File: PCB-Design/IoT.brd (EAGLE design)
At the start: 161.3 x 101.3 mm, 10 parts, among them M2 ARDUINO-NANO-3.0, M3 WIRELESS-NRF24L01

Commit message: WIP: PCB routing
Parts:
- moved U$1 49.6 mm to (44.5, 53.3)
- moved U$2 49.5 mm to (6.35, 53.3)
- moved U$4 49.5 mm to (31.8, 53.3)
- moved U$3 49.5 mm to (19.1, 53.3)
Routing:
- net N$8: track 59.0 -> 9.45 mm
- net N$7: track 59.0 -> 9.50 mm
- net N$11: track 60.6 -> 11.5 mm
- net N$6: track 61.6 -> 12.6 mm
- net N$10: track 60.6 -> 11.6 mm
- net N$5: track 61.6 -> 12.7 mm
- net N$19: track 121.2 -> 75.1 mm
- net N$12: track 63.2 -> 17.6 mm
- net N$13: track 63.2 -> 17.7 mm
- net N$15: track 35.0 -> 40.3 mm
- net N$9: track 36.9 -> 40.8 mm
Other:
- board size 161.3 x 101.3 mm -> 58.4 x 51.7 mm

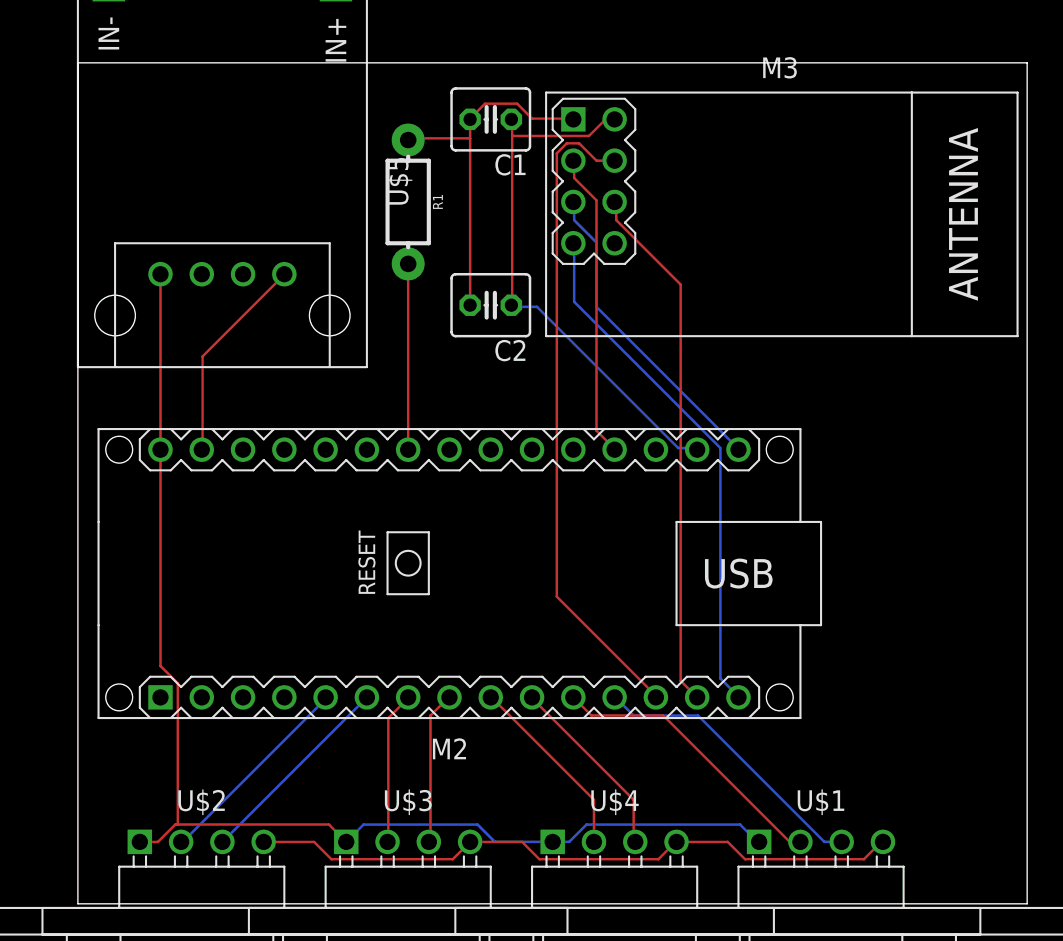
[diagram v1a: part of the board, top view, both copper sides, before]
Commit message: schematic - fixed mosfet and tidy up, board - manually routed (auto route super scary results)
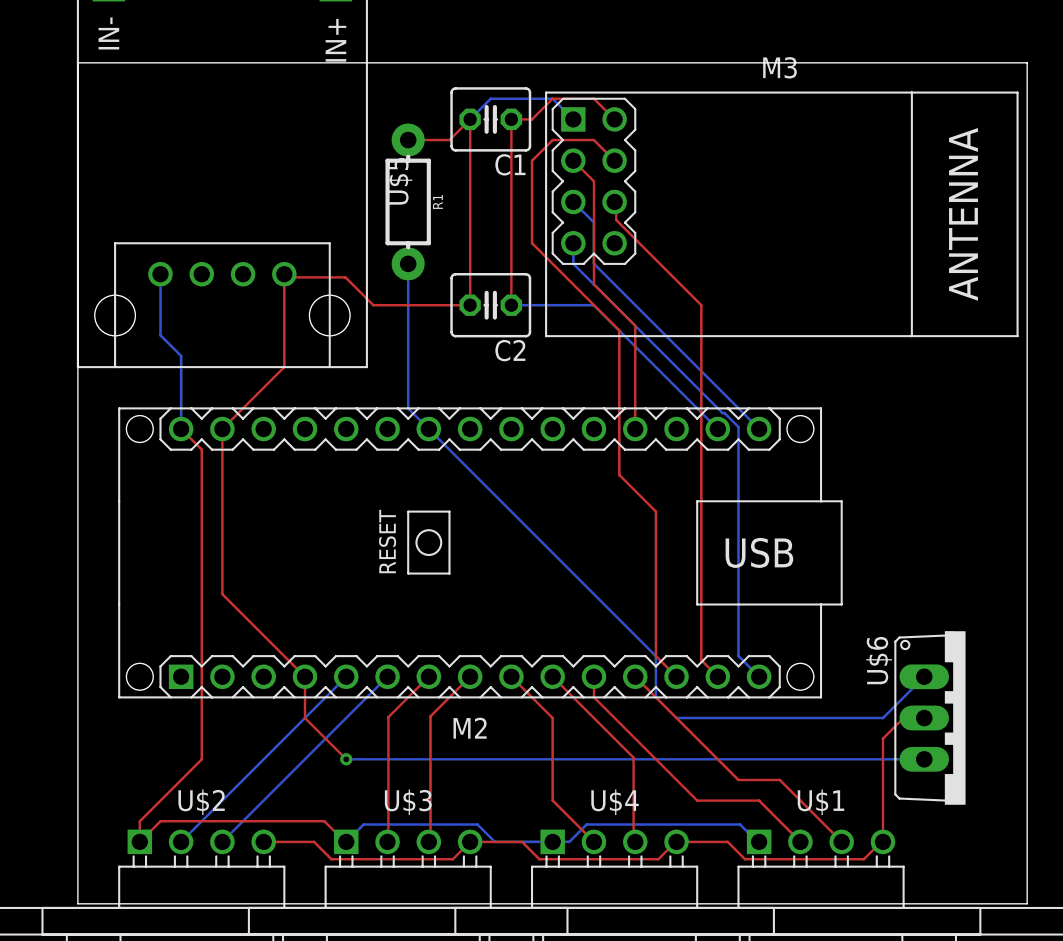
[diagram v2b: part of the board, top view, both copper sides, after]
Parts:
- added U$6: IRL520N, IRL520N:TO220-VERT
- moved M2 1.80 mm to (22.9, 71.1)
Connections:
- net N$19 renamed VCC
- removed net 3.3V: C1.2, C2.2, M3.1, R1.P$1
- removed net GND.1: M2.J1.4
- removed net N$2: M2.J2.2, U$5.GND
- new net GND: C1.2, C2.2, M2.J1.4, M2.J2.2, M3.1, R1.P$1, U$5.GND, U$6.3
- net N$1: now also U$6.1
- net N$9: now also U$6.2
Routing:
- net GND: track 0.00 -> 105.5 mm, vias 0 -> 1
- net N$1: track 11.4 -> 51.1 mm
- net 3.3V: track 22.5 -> 0.00 mm
- net N$2: track 12.9 -> 0.00 mm
- net N$9: track 40.8 -> 50.2 mm
- net VCC: track 75.1 -> 78.5 mm
- net N$8: track 9.45 -> 11.2 mm
- net N$6: track 12.6 -> 14.4 mm
- net N$7: track 9.50 -> 11.3 mm
- net N$5: track 12.7 -> 14.4 mm
- net N$4: track 33.3 -> 34.9 mm
- net N$15: track 40.3 -> 41.6 mm
- net N$14: track 18.9 -> 18.1 mm
- net N$17: track 32.6 -> 31.9 mm
- net N$10: track 11.6 -> 12.3 mm
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
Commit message: updated names on board
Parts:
- renumbered U$1 to HC-SR04-4, U$2 to HC-SR04-1, U$3 to HC-SR04-2, U$4 to HC-SR04-3
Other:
- board size 58.4 x 51.7 mm -> 59.7 x 51.7 mm

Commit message: more edits
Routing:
- net N$12: track 16.9 -> 17.7 mm
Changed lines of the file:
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@@
 <wire x1="32.0374" y1="84.8026" x2="32.0374" y2="75.9126" width="0.1524" layer="1"/>
 <wire x1="26.67" y1="90.17" x2="32.0374" y2="84.8026" width="0.1524" layer="1"/>
-<wire x1="32.0374" y1="75.9126" x2="34.29" y2="73.66" width="0.1524" layer="1"/>
-<wire x1="34.29" y1="73.66" x2="34.29" y2="64.77" width="0.1524" layer="1"/>
-<wire x1="34.29" y1="64.77" x2="35.56" y2="63.5" width="0.1524" layer="1"/>
+<wire x1="32.0374" y1="75.9126" x2="35.56" y2="72.39" width="0.1524" layer="1"/>
+<wire x1="35.56" y1="72.39" x2="35.56" y2="64.77" width="0.1524" layer="1"/>
+<wire x1="35.56" y1="64.77" x2="35.56" y2="63.5" width="0.1524" layer="1"/>
 </signal>
 <signal name="N$16">
@@
 <contactref element="HC-SR04-4" pad="3"/>
 <contactref element="M2" pad="J1.12"/>
-<wire x1="33.02" y1="63.5" x2="39.37" y2="57.15" width="0.1524" layer="1"/>
-<wire x1="39.37" y1="57.15" x2="41.91" y2="57.15" width="0.1524" layer="1"/>
+<wire x1="33.02" y1="62.23" x2="38.1" y2="57.15" width="0.1524" layer="1"/>
+<wire x1="38.1" y1="57.15" x2="41.91" y2="57.15" width="0.1524" layer="1"/>
 <wire x1="41.91" y1="57.15" x2="45.72" y2="53.34" width="0.1524" layer="1"/>
+<wire x1="33.02" y1="63.5" x2="33.02" y2="62.23" width="0.1524" layer="1"/>
 </signal>
 <signal name="N$13">
@@
 <wire x1="12.7" y1="60.96" x2="15.24" y2="58.42" width="0.1524" layer="1"/>
 <wire x1="12.7" y1="63.5" x2="12.7" y2="60.96" width="0.1524" layer="1"/>
-<wire x1="22.86" y1="97.79" x2="22.86" y2="86.36" width="0.1524" layer="1"/>
 <wire x1="19.05" y1="96.52" x2="21.59" y2="96.52" width="0.1524" layer="1"/>
 <wire x1="11.43" y1="88.265" x2="11.6278" y2="88.0672" width="0.1524" layer="1"/>
-<wire x1="16.901375" y1="86.36" x2="22.86" y2="86.36" width="0.1524" layer="1"/>
-<wire x1="11.6278" y1="88.0672" x2="15.194175" y2="88.0672" width="0.1524" layer="1"/>
-<wire x1="15.194175" y1="88.0672" x2="16.901375" y2="86.36" width="0.1524" layer="1"/>
 <wire x1="11.43" y1="82.55" x2="11.43" y2="88.265" width="0.1524" layer="1"/>
 <wire x1="7.62" y1="78.74" x2="11.43" y2="82.55" width="0.1524" layer="1"/>
@@
 <wire x1="15.24" y1="58.42" x2="50.8" y2="58.42" width="0.1524" layer="16"/>
 <wire x1="21.59" y1="96.52" x2="22.86" y2="97.79" width="0.1524" layer="1"/>
+<wire x1="11.43" y1="90.805" x2="17.145" y2="96.52" width="0.1524" layer="1"/>
+<wire x1="11.43" y1="88.265" x2="11.43" y2="90.805" width="0.1524" layer="1"/>
+<wire x1="17.145" y1="96.52" x2="19.05" y2="96.52" width="0.1524" layer="1"/>
+<wire x1="22.86" y1="86.36" x2="22.86" y2="95.25" width="0.1524" layer="1"/>
+<wire x1="22.86" y1="95.25" x2="21.59" y2="96.52" width="0.1524" layer="1"/>
 </signal>
 <signal name="VCC">
@@
 <wire x1="15.24" y1="53.34" x2="16.3068" y2="54.4068" width="0.1524" layer="16"/>
 <wire x1="15.125" y1="53.375" x2="15.24" y2="53.34" width="0.1524" layer="1"/>
-<wire x1="5.08" y1="83.235" x2="3.81" y2="84.505" width="0.1524" layer="16"/>
-<wire x1="5.08" y1="78.74" x2="5.08" y2="83.235" width="0.1524" layer="16"/>
-<wire x1="3.81" y1="84.505" x2="3.81" y2="88.265" width="0.1524" layer="16"/>
 <wire x1="6.35" y1="77.47" x2="6.35" y2="58.42" width="0.1524" layer="1"/>
 <wire x1="2.54" y1="54.61" x2="2.54" y2="53.34" width="0.1524" layer="1"/>
@@
 <wire x1="13.89" y1="54.61" x2="15.125" y2="53.375" width="0.1524" layer="1"/>
 <wire x1="5.08" y1="78.74" x2="6.35" y2="77.47" width="0.1524" layer="1"/>
+<wire x1="5.08" y1="86.995" x2="5.08" y2="78.9120375" width="0.1524" layer="1"/>
+<wire x1="5.08" y1="78.9120375" x2="5.08" y2="78.74" width="0.1524" layer="1"/>
+<wire x1="3.81" y1="88.265" x2="5.08" y2="86.995" width="0.1524" layer="1"/>
 </signal>
 </signals>
